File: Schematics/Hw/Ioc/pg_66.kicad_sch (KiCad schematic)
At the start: 12 parts, among them U6601 F113, U6602 F113, U6603 F175, U6604 F04, U6605 F240, U6606 F51

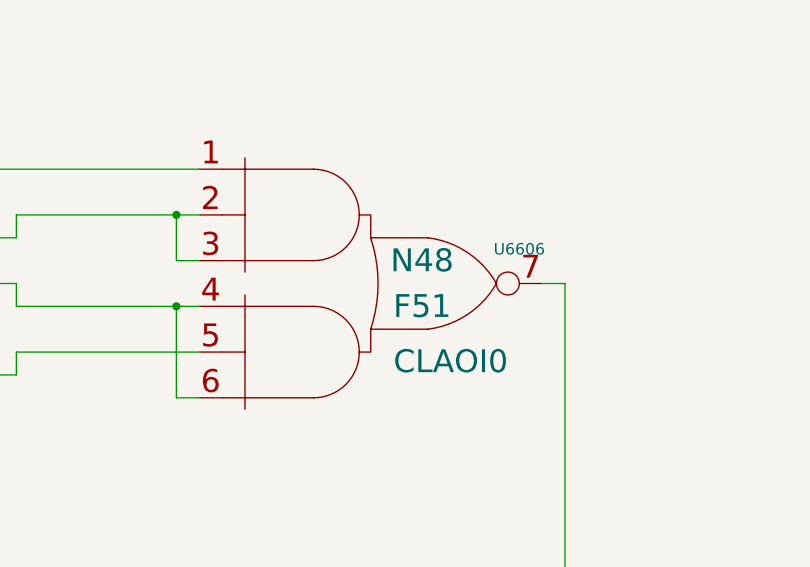
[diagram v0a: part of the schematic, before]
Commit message: Upgrade to KiCad9
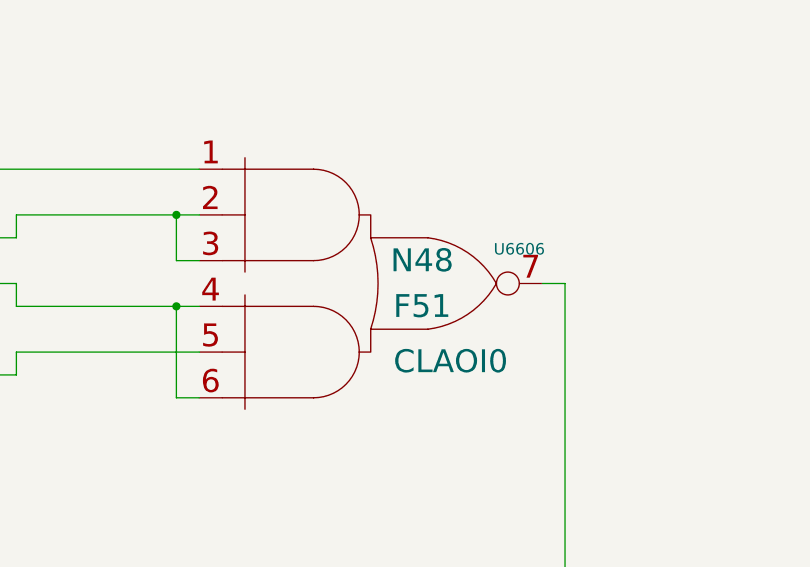
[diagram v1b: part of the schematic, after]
